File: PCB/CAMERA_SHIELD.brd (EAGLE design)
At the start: 79.7 x 100.3 mm, 72 parts, among them IC4 LSF0204PWR, J1 47346-0001, Q1 FDN304P, Q2 FDN304P, Q3 SSM3J338R,LF, Q4 SSM3J338R,LF, U1 LARA-R2

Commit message: new route
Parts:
- moved R17 10.8 mm to (7.40, 38.8), turned to 90 degrees
- moved R11 4.62 mm to (42.6, 23.1)
- moved R12 1.89 mm to (42.5, 25.0)
- moved R23 1.76 mm to (42.5, 20.3)
- moved R22 1.74 mm to (42.6, 21.7)
- moved C17 0.79 mm to (13.7, 33.6)
- moved TVS8 0.79 mm to (13.7, 36.1)
- moved C14 0.79 mm to (13.6, 31.6)
- moved C15 0.79 mm to (13.7, 34.8)
- moved C24 0.79 mm to (13.7, 32.7)
- moved ANT2 0.13 mm to (6.12, 20.7)
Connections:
- removed net RX: IC4.3, RXD.TP
- removed net TX: IC4.2, TXD.TP
- new net N$11: RTS.TP
- new net N$13: RXD.TP
- new net N$4: CTS.TP
- net CTS: now also IC4.2; no longer CTS.TP, IC4.4
- net RTS: now also IC4.3; no longer IC4.5, RTS.TP
- net RXD: now also IC4.5
- net TXD: now also IC4.4, TXD.TP
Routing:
- net VBAT: track 22.6 -> 149.8 mm
- net V_GSM: track 0.00 -> 27.3 mm
- net USART2_CTS: track 0.00 -> 16.6 mm
- net USART2_RTS: track 0.00 -> 15.1 mm
- net USART2_TX: track 0.00 -> 13.5 mm
- net USART2_RX: track 0.00 -> 8.72 mm
- net ANT: track 0.00 -> 4.53 mm
- net GSM_EN: track 0.00 -> 2.88 mm

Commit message: new 1
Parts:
- moved R11 3.13 mm to (42.5, 26.2)
- moved R23 2.72 mm to (42.5, 23.0)
- moved IC4 1.46 mm to (45.5, 11.9), turned to 0 degrees
- moved R12 0.52 mm to (42.5, 24.5)
- moved R22 0.34 mm to (42.6, 21.3)
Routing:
- net USART2_CTS: track 16.6 -> 36.9 mm, vias 0 -> 2
- net USART2_RTS: track 15.1 -> 34.2 mm, vias 0 -> 2
- net USART2_TX: track 13.5 -> 31.8 mm, vias 0 -> 2
- net USART2_RX_P: track 0.00 -> 17.8 mm
- net USART2_RX: track 8.72 -> 25.3 mm, vias 0 -> 2
- net USART2_RTS_P: track 0.00 -> 15.2 mm, vias 0 -> 2
- net USART2_TX_P: track 0.00 -> 14.2 mm
- net USART2_CTS_P: track 0.00 -> 12.8 mm

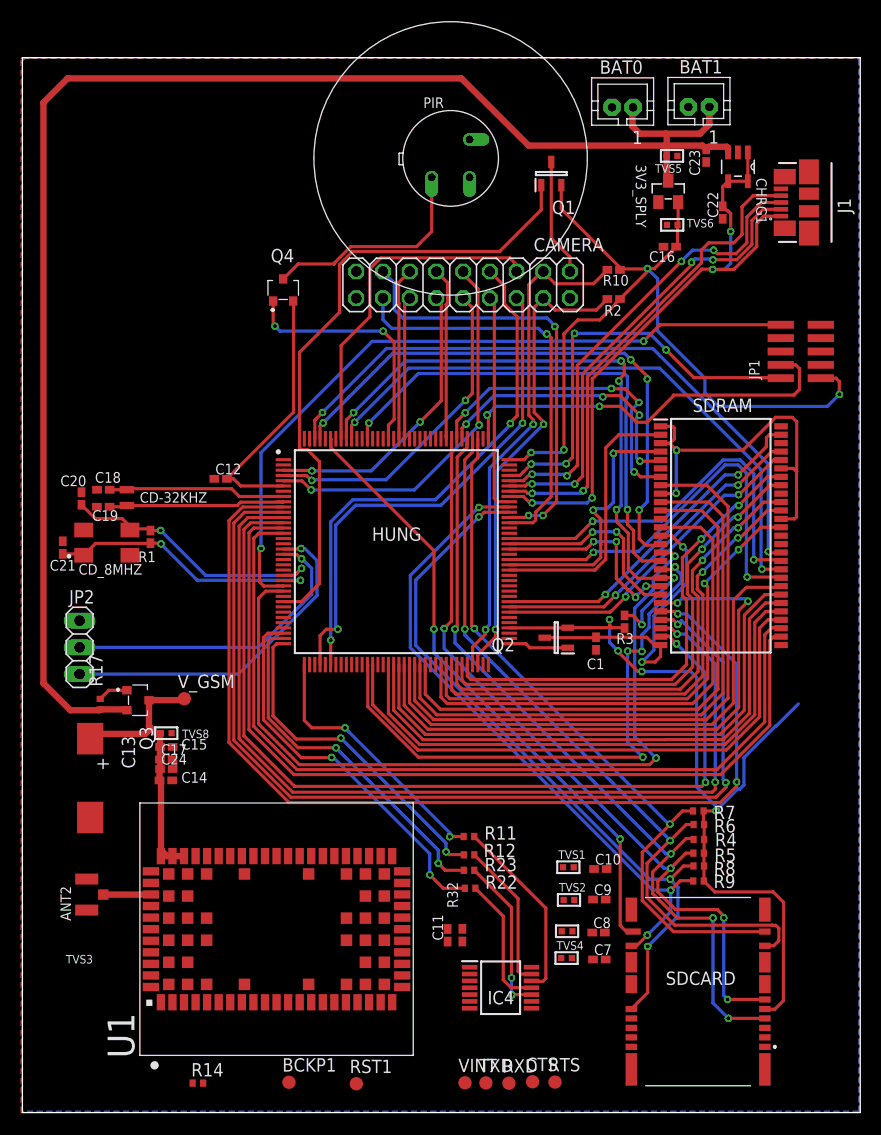
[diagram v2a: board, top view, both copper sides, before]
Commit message: route gsm
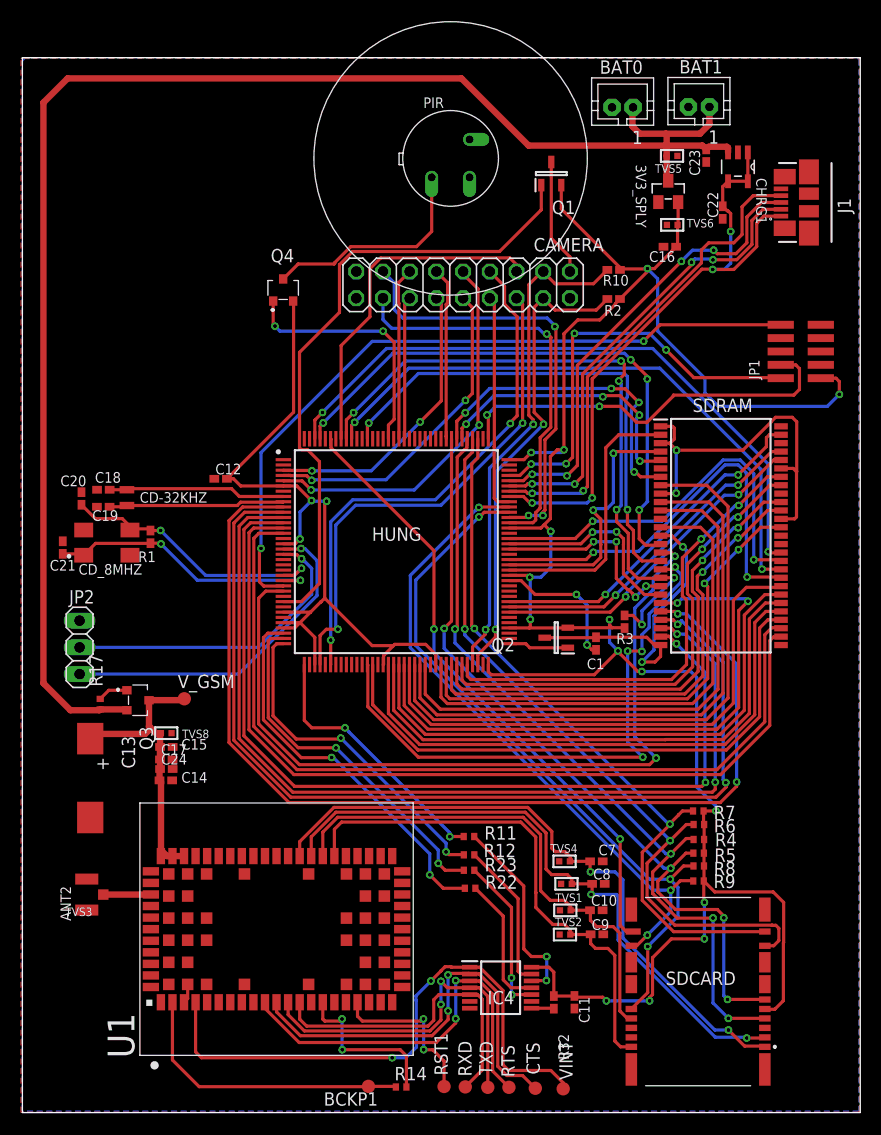
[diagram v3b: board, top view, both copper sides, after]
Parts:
- moved R14 19.3 mm to (36.0, 2.43)
- moved C11 13.6 mm to (52.5, 10.5), turned to 270 degrees
- moved R32 10.8 mm to (50.5, 10.5), turned to 270 degrees
- moved VINT 9.36 mm to (51.4, 2.26)
- moved C7 9.33 mm to (54.6, 23.9)
- moved TVS4 9.20 mm to (51.6, 23.9)
- moved RST1 8.34 mm to (40.1, 2.48)
- moved BCKP1 7.57 mm to (32.9, 2.49)
- moved C8 4.63 mm to (54.8, 21.8)
- moved TVS3 4.51 mm to (51.7, 21.8)
- moved RTS 4.41 mm to (46.3, 2.40)
- moved RXD 4.16 mm to (42.1, 2.44)
- moved TVS1 4.11 mm to (51.6, 19.2)
- moved C10 3.94 mm to (54.6, 19.2)
- moved C9 3.32 mm to (54.6, 16.9)
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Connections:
- removed net N$11: RTS.TP
- removed net N$13: RXD.TP
- removed net N$3: SDCARD.1
- removed net N$4: CTS.TP
- removed net N$5: SDCARD.3
- removed net N$6: SDCARD.2
- removed net N$8: SDCARD.4
- removed net N$9: SDCARD.6
- removed net SIGNAL_C1: C7.1, TVS4.2
- removed net SIGNAL_C2: C8.1, TVS3.2
- removed net SIGNAL_C3: C9.1, TVS2.2
- removed net SIGNAL_C7: C10.1, TVS1.2
- removed net VIN: U1.4
- net CTS: now also CTS.TP
- net RTS: now also RTS.TP
- net RXD: now also RXD.TP
- net SIM_CLK: now also C9.1, SDCARD.3, TVS2.2
- net SIM_IO: now also C10.1, SDCARD.6, TVS1.2
- net SIM_RST: now also C8.1, SDCARD.2, TVS3.2
- net VSIM: now also C7.1, SDCARD.1, TVS4.2
- net V_INT: now also U1.4
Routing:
- net 3V3: track 183.3 -> 288.2 mm, vias 8 -> 18
- net VSIM: track 0.00 -> 61.4 mm, vias 0 -> 2
- net SIM_RST: track 0.00 -> 60.3 mm, vias 0 -> 2
- net V_INT: track 0.00 -> 55.7 mm, vias 0 -> 2
- net SIM_CLK: track 0.00 -> 49.4 mm
- net SIM_IO: track 0.00 -> 48.3 mm
- net CTS: track 0.00 -> 40.1 mm, vias 0 -> 2
- net RTS: track 0.00 -> 38.4 mm, vias 0 -> 2
- net TXD: track 0.00 -> 34.2 mm, vias 0 -> 2
- net RXD: track 0.00 -> 30.8 mm
- net V_BCKP_SIG: track 0.00 -> 27.8 mm
- net GSM_PWR_ON1: track 0.00 -> 15.8 mm, vias 0 -> 2
- net GSM_RESET_N: track 0.00 -> 15.6 mm, vias 0 -> 2
- net GND: track 0.00 -> 15.1 mm, vias 0 -> 2
- net N$12: track 0.00 -> 2.14 mm
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
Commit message: stm32f7 with gsm-modul
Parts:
- added Q5: FDN304P, FDN304P:SOT95P237X112-3N
- moved C7 0.52 mm to (54.6, 24.4)
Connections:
- removed net PIR_IN: HUNG.127
- new net 3V3_SDCARD: Q5.3, SDCARD.10
- net 3V3: now also HUNG.121, HUNG.144, Q5.2; no longer SDCARD.10
- net MOSFET_SDCARD: now also Q5.1
- net PIR_INT: now also HUNG.127
- net VDD: no longer HUNG.121, HUNG.144
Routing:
- net GND: track 15.1 -> 114.4 mm, vias 2 -> 16
- net MOSFET_SDCARD: track 0.00 -> 55.5 mm, vias 0 -> 2
- net PIR_INT: track 0.00 -> 34.5 mm, vias 0 -> 2
- net 3V3_SDCARD: track 0.00 -> 19.8 mm, vias 0 -> 2
- net 3V3: track 288.2 -> 296.2 mm, vias 18 -> 22
- net 3V3_SDRAM: track 65.4 -> 71.8 mm, vias 4 -> 8
- net SIM_IO: track 48.3 -> 53.6 mm, vias 0 -> 2
- net FMC_A0: track 99.0 -> 100.0 mm
- net FMC_A1: track 95.2 -> 96.1 mm
- net FMC_A4: track 84.7 -> 85.6 mm
- net FMC_A5: track 83.2 -> 84.0 mm
- net FMC_SDNWE: track 77.4 -> 78.1 mm
- net FMC_A3: track 85.9 -> 86.6 mm
- net FMC_A2: track 91.0 -> 91.6 mm
- net USART2_CTS: track 36.9 -> 37.4 mm

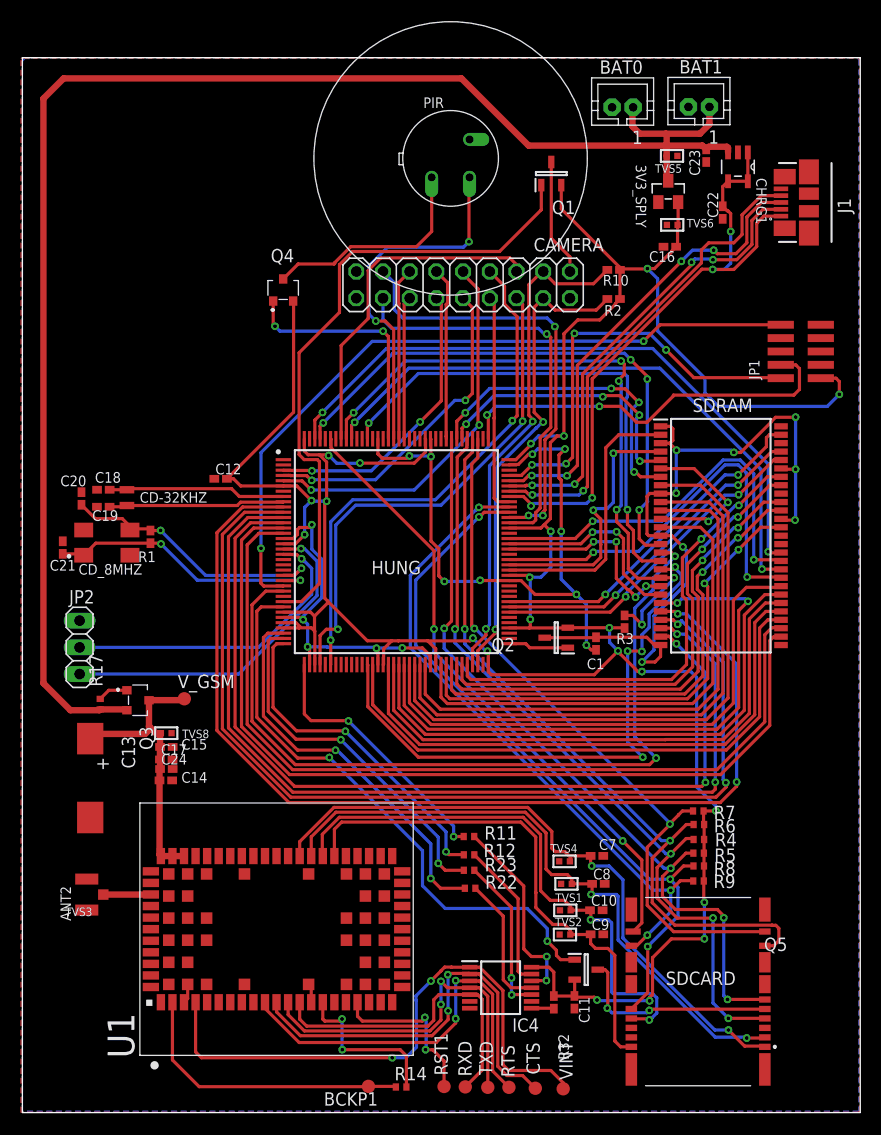
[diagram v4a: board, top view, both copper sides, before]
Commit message: fix gsm-modul
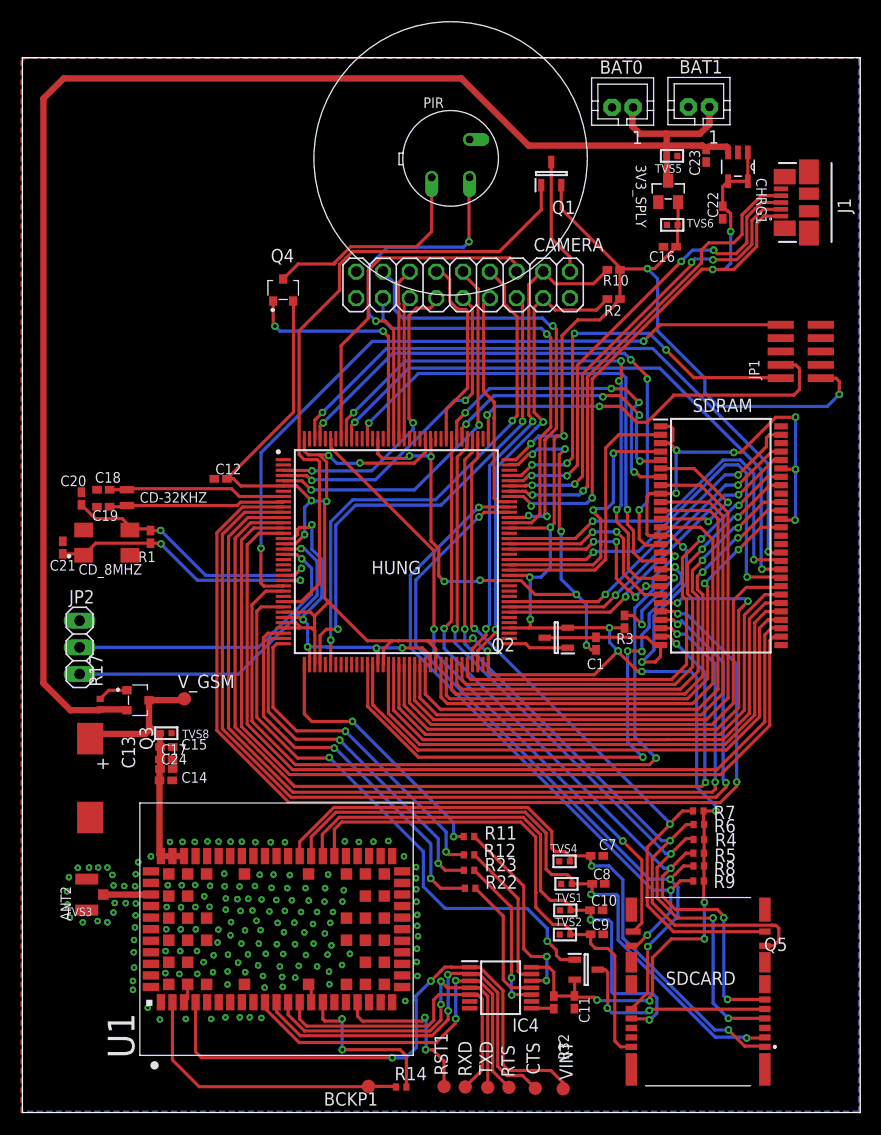
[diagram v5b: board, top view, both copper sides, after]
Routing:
- net DCMI_D5: track 16.4 -> 18.7 mm
- net DCMI_D4: track 27.7 -> 28.5 mm

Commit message: smartcamera with gsm
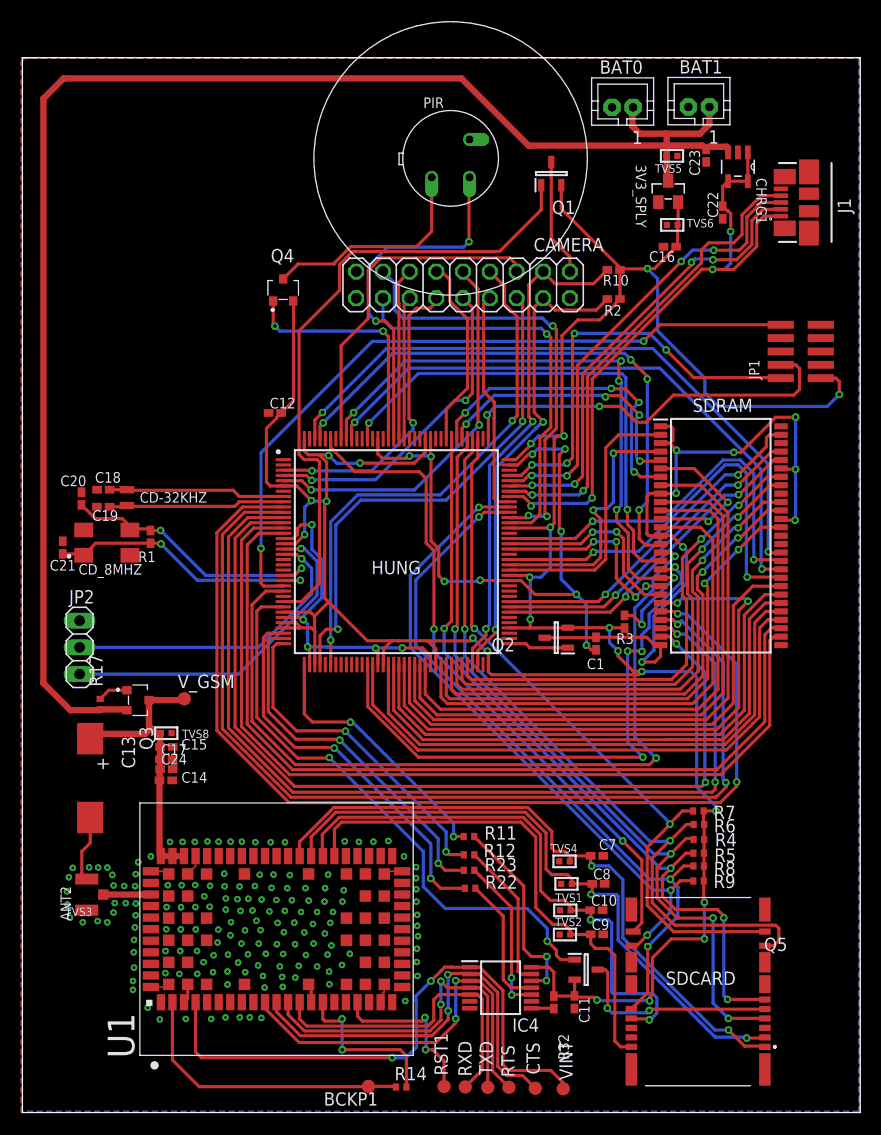
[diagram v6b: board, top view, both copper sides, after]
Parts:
- moved C12 8.11 mm to (24.0, 66.5)
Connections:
- new net N$196: U1.51, U1.52, U1.53
- net V_GSM: no longer U1.51, U1.52, U1.53
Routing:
- net GND: track 114.4 -> 130.2 mm
- net CARD_DET: track 59.5 -> 63.1 mm
- net 3V3: track 296.3 -> 293.0 mm
- net V_GSM: track 27.6 -> 25.2 mm
- net N$196: track 0.00 -> 2.20 mm
- net SDIO_D3: track 72.3 -> 73.1 mm
- net SDIO_CK: track 76.0 -> 76.7 mm

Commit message: fix router
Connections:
- removed net N$196: U1.51, U1.52, U1.53
- net V_GSM: now also U1.51, U1.52, U1.53
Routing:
- net V_GSM: track 25.2 -> 27.6 mm
- net N$196: track 2.20 -> 0.00 mm
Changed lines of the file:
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@@
 <wire x1="54.873" y1="67.1612" x2="56.8828875" y2="67.1612" width="0.3048" layer="1"/>
 <wire x1="72.12" y1="71.1" x2="72.12" y2="71.11" width="0.3048" layer="1"/>
-<wire x1="59.37" y1="65.61" x2="59.333" y2="65.647" width="0.3048" layer="1"/>
 <wire x1="58.3970875" y1="65.647" x2="59.333" y2="65.647" width="0.3048" layer="1"/>
 <wire x1="56.8828875" y1="67.1612" x2="58.3970875" y2="65.647" width="0.3048" layer="1"/>
@@
 <contactref element="V_GSM" pad="TP"/>
 <contactref element="TVS8" pad="2"/>
+<contactref element="U1" pad="52"/>
+<contactref element="U1" pad="53"/>
+<contactref element="U1" pad="51"/>
 <contactref element="Q3" pad="3"/>
 <wire x1="15.4" y1="39.35" x2="15.27" y2="39.22" width="0.6096" layer="1"/>
@@
 <wire x1="13.09" y1="32.67" x2="13.09" y2="33.57" width="0.6096" layer="1"/>
 <wire x1="13.09" y1="33.57" x2="13.08" y2="33.58" width="0.6096" layer="1"/>
+<wire x1="14.27" y1="24.39" x2="15.37" y2="24.39" width="0.6096" layer="1"/>
+<wire x1="13.17" y1="24.39" x2="14.27" y2="24.39" width="0.6096" layer="1"/>
 <wire x1="13.04" y1="31.59" x2="13.04" y2="24.52" width="0.6096" layer="1"/>
-<wire x1="13.04" y1="31.59" x2="13.04" y2="32.62" width="0.6096" layer="1"/>
-<wire x1="13.04" y1="32.62" x2="13.09" y2="32.67" width="0.6096" layer="1"/>
+<wire x1="13.04" y1="24.52" x2="13.17" y2="24.39" width="0.6096" layer="1"/>
+<wire x1="13.09" y1="32.67" x2="13.09" y2="31.64" width="0.6096" layer="1"/>
+<wire x1="13.09" y1="31.64" x2="13.04" y2="31.59" width="0.6096" layer="1"/>
 </signal>
 <signal name="USART2_CTS">
@@
 <via x="10.62" y="13.79" extent="1-16" drill="0.25"/>
 </signal>
-<signal name="N$196">
-<contactref element="U1" pad="52"/>
-<contactref element="U1" pad="53"/>
-<contactref element="U1" pad="51"/>
-<wire x1="14.27" y1="24.39" x2="15.37" y2="24.39" width="0.6096" layer="1"/>
-<wire x1="13.17" y1="24.39" x2="14.27" y2="24.39" width="0.6096" layer="1"/>
-</signal>
 </signals>

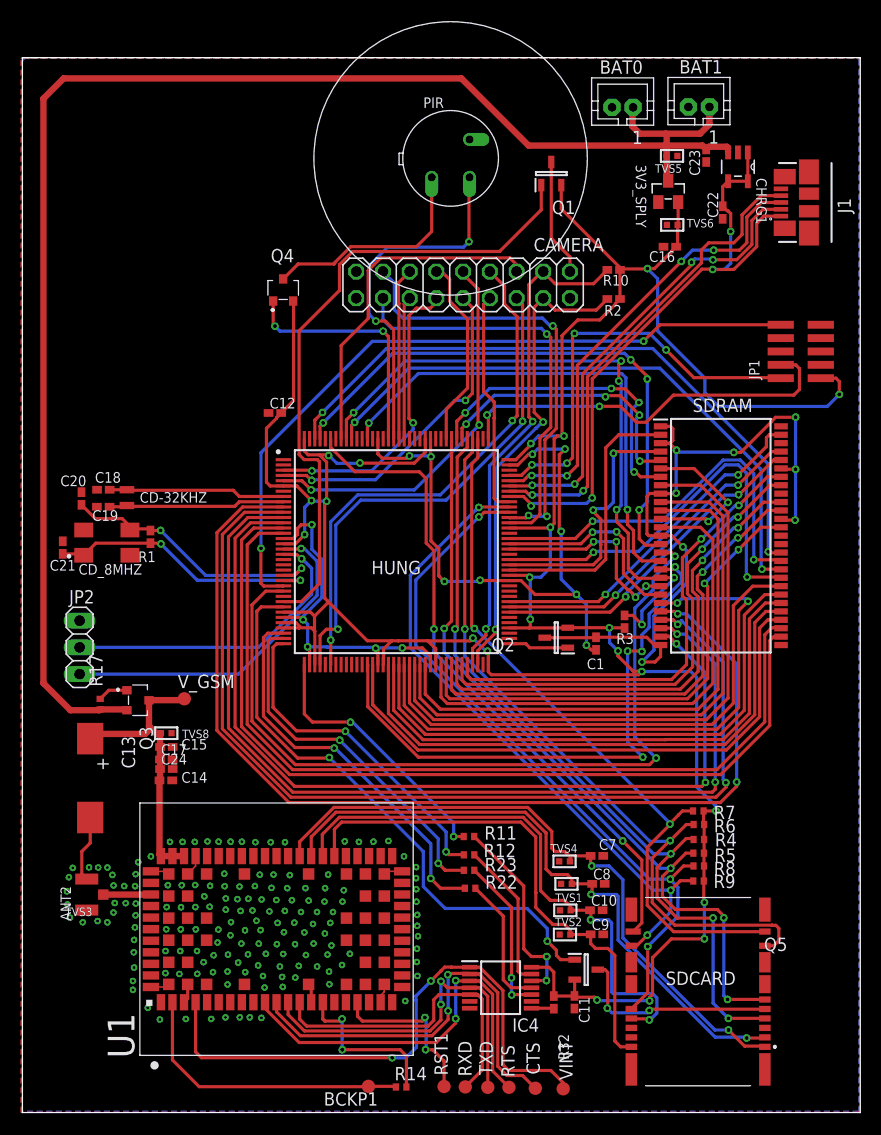
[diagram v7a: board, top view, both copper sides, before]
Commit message: fix ERC-Fehler
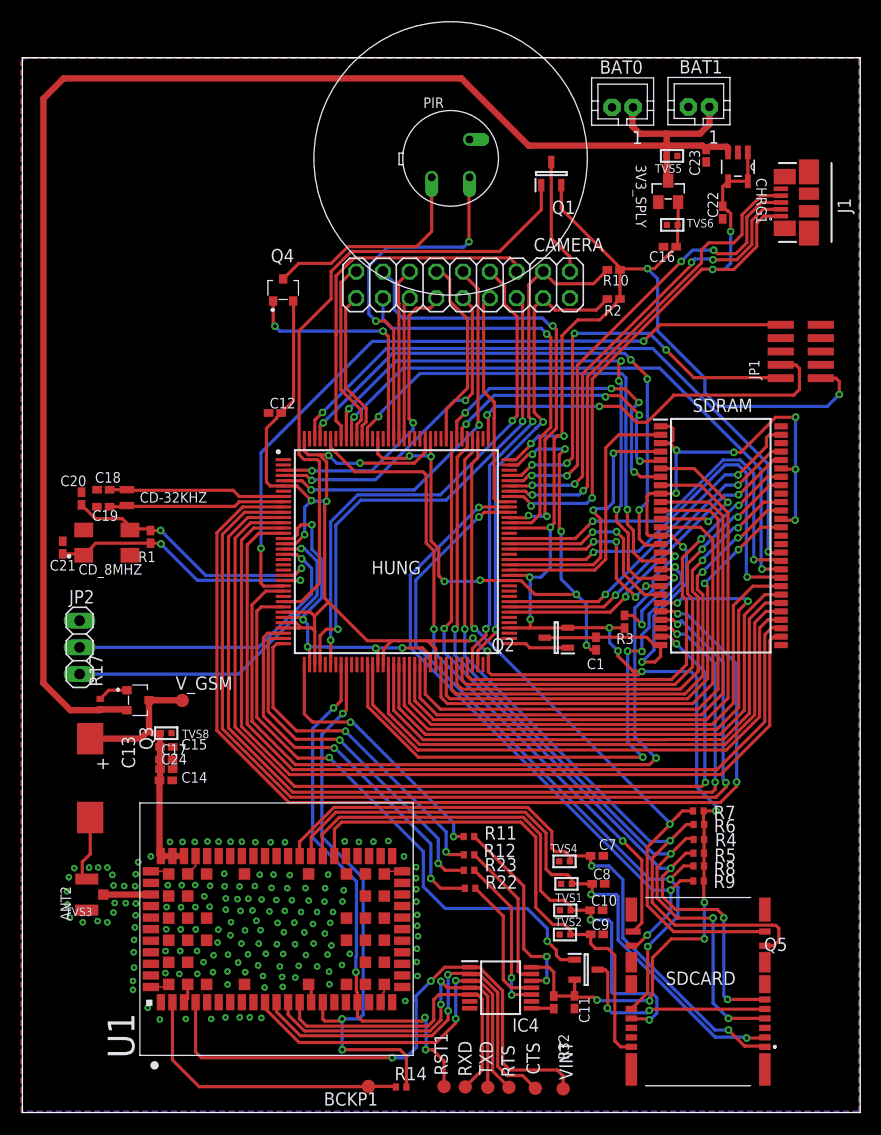
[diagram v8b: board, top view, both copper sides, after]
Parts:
- moved V_GSM 0.26 mm to (15.2, 39.2)
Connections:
- removed net GSM_PWR_ON1: R14.2, U1.15
- removed net N$119: HUNG.134
- removed net N$120: HUNG.133
- removed net N$44: HUNG.44
- removed net N$45: HUNG.45
- removed net N$98: HUNG.83
- removed net N$99: HUNG.82
- removed net VSS: C12.1
- new net GSM_PWR_ON: HUNG.45, R14.2, U1.15
- net GND: now also C12.1
- net GSM_RESET_N: now also HUNG.44
- net PWDN: now also HUNG.133
- net RESET: now also HUNG.134
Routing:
- net GSM_PWR_ON: track 0.00 -> 53.9 mm, vias 0 -> 3
- net GSM_RESET_N: track 15.9 -> 51.0 mm, vias 2 -> 4
- net RESET: track 0.00 -> 17.7 mm
- net GSM_PWR_ON1: track 15.8 -> 0.00 mm, vias 2 -> 0
- net PWDN: track 0.00 -> 14.7 mm
- net DCMI_VSYNC: track 32.6 -> 34.5 mm
- net FMC_SDNE1: track 63.4 -> 63.9 mm
